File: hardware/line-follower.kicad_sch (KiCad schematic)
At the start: 45 parts, among them J1 AVR-ISP-6, U1 QRE1113GR, U10 QRE1113GR, U11 ATmega2560-16A, U2 QRE1113GR, U3 QRE1113GR, U4 QRE1113GR, U5 QRE1113GR, U6 QRE1113GR, U7 QRE1113GR, U8 QRE1113GR, U9 QRE1113GR

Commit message: add hole for fan
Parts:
- J1: footprint (none) -> Connector_PinHeader_2.54mm:PinHeader_2x03_P2.54mm_Vertical
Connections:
- net +5V: now also J1.2 (VCC)
- net GND: now also J1.6 (GND), U11.11 (GND), U11.32 (GND), U11.62 (GND), U11.81 (GND), U11.99 (GND)
- net at U11.10 (VCC), U11.31 (VCC), U11.61 (VCC)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: now also C11.2, C12.2, C13.2
- net SCK: now reaches U11.20 (PB1)
- net SCK: now also J1.3 (SCK)
- net MOSI: now reaches U11.21 (PB2)
- net MOSI: now also J1.4 (MOSI)
- net MISO: now reaches U11.22 (PB3)
- net MISO: now also J1.1 (MISO)
- net RESET: now reaches U11.30 (~{RESET})
- net RESET: now also J1.5 (~{RST})
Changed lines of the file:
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@@
 (kicad_sch (version 20230121) (generator eeschema)
   (paper "A4")
+  (junction (at 50.8 24.13) (diameter 0) (color 0 0 0 0)
+  )
   (junction (at 226.06 62.23) (diameter 0) (color 0 0 0 0)
   )
+  (junction (at 59.69 24.13) (diameter 0) (color 0 0 0 0)
+  )
   (junction (at 269.24 62.23) (diameter 0) (color 0 0 0 0)
   )
@@
   (junction (at 182.88 62.23) (diameter 0) (color 0 0 0 0)
   )
+  (junction (at 41.91 24.13) (diameter 0) (color 0 0 0 0)
+  )
   (junction (at 269.24 29.21) (diameter 0) (color 0 0 0 0)
   )
@@
     (stroke (width 0) (type default))
   )
+  (wire (pts (xy 67.31 24.13) (xy 67.31 33.02))
+    (stroke (width 0) (type default))
+  )
   (wire (pts (xy 165.1 29.21) (xy 166.37 29.21))
     (stroke (width 0) (type default))
@@
     (stroke (width 0) (type default))
   )
+  (wire (pts (xy 114.3 21.59) (xy 119.38 21.59))
+    (stroke (width 0) (type default))
+  )
   (wire (pts (xy 269.24 87.63) (xy 269.24 88.9))
     (stroke (width 0) (type default))
@@
     (stroke (width 0) (type default))
   )
+  (wire (pts (xy 142.24 21.59) (xy 146.05 21.59))
+    (stroke (width 0) (type default))
+  )
   (wire (pts (xy 224.79 67.31) (xy 227.33 67.31))
     (stroke (width 0) (type default))
@@
     (stroke (width 0) (type default))
   )
+  (wire (pts (xy 59.69 24.13) (xy 67.31 24.13))
+    (stroke (width 0) (type default))
+  )
   (wire (pts (xy 275.59 95.25) (xy 276.86 95.25))
     (stroke (width 0) (type default))
@@
     (stroke (width 0) (type default))
   )
+  (wire (pts (xy 114.3 25.4) (xy 114.3 21.59))
+    (stroke (width 0) (type default))
+  )
   (wire (pts (xy 269.24 54.61) (xy 269.24 55.88))
     (stroke (width 0) (type default))
@@
     (stroke (width 0) (type default))
   )
+  (wire (pts (xy 41.91 24.13) (xy 50.8 24.13))
+    (stroke (width 0) (type default))
+  )
   (wire (pts (xy 252.73 100.33) (xy 250.19 100.33))
     (stroke (width 0) (type default))
@@
     (stroke (width 0) (type default))
   )
+  (wire (pts (xy 41.91 24.13) (xy 39.37 24.13))
+    (stroke (width 0) (type default))
+  )
   (wire (pts (xy 207.01 100.33) (xy 207.01 101.6))
     (stroke (width 0) (type default))
@@
     (stroke (width 0) (type default))
   )
+  (wire (pts (xy 146.05 21.59) (xy 146.05 19.05))
+    (stroke (width 0) (type default))
+  )
   (wire (pts (xy 158.75 54.61) (xy 158.75 62.23))
     (stroke (width 0) (type default))
   )
+  (wire (pts (xy 39.37 20.32) (xy 39.37 24.13))
+    (stroke (width 0) (type default))
+  )
   (wire (pts (xy 250.19 34.29) (xy 250.19 35.56))
     (stroke (width 0) (type default))
@@
   )
   (wire (pts (xy 201.93 62.23) (xy 203.2 62.23))
+    (stroke (width 0) (type default))
+  )
+  (wire (pts (xy 50.8 24.13) (xy 59.69 24.13))
     (stroke (width 0) (type default))
   )
@@
     )
   )
+  (global_label "MISO" (shape input) (at 134.62 34.29 270) (fields_autoplaced)
+    (effects (font (size 1.27 1.27)) (justify right))
+    (property "Intersheetrefs" "${INTERSHEET_REFS}" (at 134.62 41.792 90)
+      (effects (font (size 1.27 1.27)) (justify right) hide)
+    )
+  )
   (global_label "OUT7" (shape input) (at 233.68 95.25 0) (fields_autoplaced)
     (effects (font (size 1.27 1.27)) (justify left))
@@
     )
   )
+  (global_label "MOSI" (shape input) (at 87.63 68.58 0) (fields_autoplaced)
+    (effects (font (size 1.27 1.27)) (justify left))
+    (property "Intersheetrefs" "${INTERSHEET_REFS}" (at 95.132 68.58 0)
+      (effects (font (size 1.27 1.27)) (justify left) hide)
+    )
+  )
   (global_label "OUT6" (shape input) (at 233.68 62.23 0) (fields_autoplaced)
     (effects (font (size 1.27 1.27)) (justify left))
@@
     )
   )
+  (global_label "MISO" (shape input) (at 87.63 71.12 0) (fields_autoplaced)
+    (effects (font (size 1.27 1.27)) (justify left))
+    (property "Intersheetrefs" "${INTERSHEET_REFS}" (at 95.132 71.12 0)
+      (effects (font (size 1.27 1.27)) (justify left) hide)
+    )
+  )
   (global_label "OUT3" (shape input) (at 276.86 95.25 0) (fields_autoplaced)
     (effects (font (size 1.27 1.27)) (justify left))
@@
     )
   )
+  (global_label "MOSI" (shape input) (at 132.08 34.29 270) (fields_autoplaced)
+    (effects (font (size 1.27 1.27)) (justify right))
+    (property "Intersheetrefs" "${INTERSHEET_REFS}" (at 132.08 41.792 90)
+      (effects (font (size 1.27 1.27)) (justify right) hide)
+    )
+  )
   (global_label "OUT8" (shape input) (at 233.68 128.27 0) (fields_autoplaced)
     (effects (font (size 1.27 1.27)) (justify left))
@@
     )
   )
+  (global_label "RESET" (shape input) (at 46.99 40.64 180) (fields_autoplaced)
+    (effects (font (size 1.27 1.27)) (justify right))
+    (property "Intersheetrefs" "${INTERSHEET_REFS}" (at 38.3391 40.64 0)
+      (effects (font (size 1.27 1.27)) (justify right) hide)
+    )
+  )
   (global_label "OUT5" (shape input) (at 87.63 165.1 0) (fields_autoplaced)
     (effects (font (size 1.27 1.27)) (justify left))
@@
     )
   )
+  (global_label "SCK" (shape input) (at 129.54 34.29 270) (fields_autoplaced)
+    (effects (font (size 1.27 1.27)) (justify right))
+    (property "Intersheetrefs" "${INTERSHEET_REFS}" (at 129.54 40.9453 90)
+      (effects (font (size 1.27 1.27)) (justify right) hide)
+    )
+  )
+  (global_label "SCK" (shape input) (at 87.63 66.04 0) (fields_autoplaced)
+    (effects (font (size 1.27 1.27)) (justify left))
+    (property "Intersheetrefs" "${INTERSHEET_REFS}" (at 94.2853 66.04 0)
+      (effects (font (size 1.27 1.27)) (justify left) hide)
+    )
+  )
   (global_label "OUT9" (shape input) (at 190.5 29.21 0) (fields_autoplaced)
     (effects (font (size 1.27 1.27)) (justify left))
     (property "Intersheetrefs" "${INTERSHEET_REFS}" (at 198.2439 29.21 0)
       (effects (font (size 1.27 1.27)) (justify left) hide)
+    )
+  )
+  (global_label "RESET" (shape input) (at 127 34.29 270) (fields_autoplaced)
+    (effects (font (size 1.27 1.27)) (justify right))
+    (property "Intersheetrefs" "${INTERSHEET_REFS}" (at 127 42.9409 90)
+      (effects (font (size 1.27 1.27)) (justify right) hide)
     )
   )
@@
       (effects (font (size 1.27 1.27)))
     )
-    (property "Footprint" "" (at 130.81 17.78 90)
+    (property "Footprint" "Connector_PinHeader_2.54mm:PinHeader_2x03_P2.54mm_Vertical" (at 130.81 17.78 90)
       (effects (font (size 1.27 1.27)) hide)
     )
@@
     )
   )
+  (symbol (lib_id "power:GND") (at 114.3 25.4 0) (unit 1)
+    (in_bom yes) (on_board yes) (dnp no) (fields_autoplaced)
+    (property "Reference" "#PWR042" (at 114.3 31.75 0)
+      (effects (font (size 1.27 1.27)) hide)
+    )
+    (property "Value" "GND" (at 114.3 30.48 0)
+      (effects (font (size 1.27 1.27)))
+    )
+    (property "Footprint" "" (at 114.3 25.4 0)
+      (effects (font (size 1.27 1.27)) hide)
+    )
+    (property "Datasheet" "" (at 114.3 25.4 0)
+      (effects (font (size 1.27 1.27)) hide)
+    )
+    (pin "1")
+    (instances
+      (project "line-follower"
+        (path "/16c7c831-eafb-4a0a-afab-2bf2c115b426"
+          (reference "#PWR042") (unit 1)
+        )
+      )
+    )
+  )
   (symbol (lib_id "power:GND") (at 163.83 35.56 0) (unit 1)
     (in_bom yes) (on_board yes) (dnp no) (fields_autoplaced)
@@
     )
   )
+  (symbol (lib_id "power:+5V") (at 146.05 19.05 0) (unit 1)
+    (in_bom yes) (on_board yes) (dnp no) (fields_autoplaced)
+    (property "Reference" "#PWR041" (at 146.05 22.86 0)
+      (effects (font (size 1.27 1.27)) hide)
+    )
+    (property "Value" "+5V" (at 146.05 13.97 0)
+      (effects (font (size 1.27 1.27)))
+    )
+    (property "Footprint" "" (at 146.05 19.05 0)
+      (effects (font (size 1.27 1.27)) hide)
+    )
+    (property "Datasheet" "" (at 146.05 19.05 0)
+      (effects (font (size 1.27 1.27)) hide)
+    )
+    (pin "1")
+    (instances
+      (project "line-follower"
+        (path "/16c7c831-eafb-4a0a-afab-2bf2c115b426"
+          (reference "#PWR041") (unit 1)
+        )
+      )
+    )
+  )
   (symbol (lib_id "power:+5V") (at 226.06 120.65 0) (unit 1)
     (in_bom yes) (on_board yes) (dnp no) (fields_autoplaced)
@@
         )
       )
+    )
+  )
+  (symbol (lib_id "power:GND") (at 67.31 180.34 0) (unit 1)
+    (in_bom yes) (on_board yes) (dnp no) (fields_autoplaced)
+    (property "Reference" "#PWR043" (at 67.31 186.69 0)
+      (effects (font (size 1.27 1.27)) hide)
+    )
+    (property "Value" "GND" (at 67.31 185.42 0)
+      (effects (font (size 1.27 1.27)))
+    )
+    (property "Footprint" "" (at 67.31 180.34 0)
+      (effects (font (size 1.27 1.27)) hide)
+    )
+    (property "Datasheet" "" (at 67.31 180.34 0)
+      (effects (font (size 1.27 1.27)) hide)
+    )
+    (pin "1")
+    (instances
+      (project "line-follower"
+        (path "/16c7c831-eafb-4a0a-afab-2bf2c115b426"
+          (reference "#PWR043") (unit 1)
+        )
+      )

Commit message: add regulator
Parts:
- added C14, C15, C21: C_Polarized_Small, Capacitor_SMD:CP_Elec_6.3x4.9, symbol Device:C_Polarized_Small
- added C16, C17: 20p, Capacitor_SMD:C_0603_1608Metric, symbol Device:C_Small
- added C18, C19, C20: 10nF, Capacitor_SMD:C_0603_1608Metric, symbol Device:C_Small
- added D1: 1N5819, Diode_THT:D_DO-41_SOD81_P10.16mm_Horizontal, symbol Diode:1N5819
- added J2, J3: Conn_01x02, Connector_PinSocket_2.54mm:PinSocket_1x02_P2.54mm_Vertical, symbol Connector_Generic:Conn_01x02
- added J4: Conn_01x02, Connector_PinHeader_2.54mm:PinHeader_1x02_P2.54mm_Vertical, symbol Connector_Generic:Conn_01x02
- added Q1: Si2319CDS, Package_TO_SOT_SMD:SOT-23, symbol Transistor_FET:Si2319CDS
- added R21: 1M, Resistor_SMD:R_0603_1608Metric, symbol Device:R_Small
- added R22, R23: R_Small, Resistor_SMD:R_0603_1608Metric, symbol Device:R_Small
- added U12: MX1508, Package_SO:SOIC-16W_5.3x10.2mm_P1.27mm, symbol MX1508:MX1508
- added U13: LM317_SOT-223, Package_TO_SOT_SMD:SOT-223-3_TabPin2, symbol Regulator_Linear:LM317_SOT-223
- added Y1: Crystal, Crystal:Crystal_SMD_HC49-SD, symbol Device:Crystal
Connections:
- net +5V: now also C11.2, C12.2, C13.2, U11.10 (VCC), U11.100 (AVCC), U11.31 (VCC), U11.61 (VCC), U11.80 (VCC), C14.1, C15.1, C18.2, C19.2, U12.1 (VCC1), U12.4 (VDD1), U12.5 (VCC2), U12.8 (VDD2), U13.2 (VO)
- net GND: now also C11.1, C12.1, C13.1, C14.2, C15.2, C16.2, C17.2, C18.1, C19.1, C20.1, C21.2, Q1.2 (S), R23.2, U12.10 (AGND2), U12.11 (PGND2), U12.14 (AGND1), U12.15 (PGND1), U13.1 (ADJ)
- net MOTOR_L_A: now reaches U11.15 (PH3)
- net MOTOR_L_A: now also U12.2 (INA1)
- net MOTOR_L_B: now reaches U11.16 (PH4)
- net MOTOR_L_B: now also U12.3 (INB1)
- net MOTOR_R_A: now reaches U11.17 (PH5)
- net MOTOR_R_A: now also U12.6 (INA2)
- net MOTOR_R_B: now reaches U11.18 (PH6)
- net MOTOR_R_B: now also U12.7 (INB2)
- net MOTOR_1: now reaches U11.23 (PB4)
- net MOTOR_1: now also R22.1
- net OSOUT: now reaches U11.33 (XTAL2)
- net OSOUT: now also C17.1, R21.2, Y1.1
- net OSIN: now reaches U11.34 (XTAL1)
- net OSIN: now also C16.1, R21.1, Y1.2
- new net: J2.2 (Pin_2), U12.13 (OUTB1)
- new net: J2.1 (Pin_1), U12.16 (OUTA1)
- new net: D1.2 (A), J4.2 (Pin_2), Q1.3 (D)
- new net: J3.1 (Pin_1), U12.12 (OUTA2)
- new net: J3.2 (Pin_2), U12.9 (OUTB2)
- new net: Q1.1 (G), R22.2, R23.1
- new net +BATT: C20.2, C21.1, D1.1 (K), J4.1 (Pin_1), U13.3 (VI)
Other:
- note added: "5V regulator"
- note added: "FAN CONTROL"
- note added: "MCU"
- note added: "MCU OSCILATOR"
- note added: "MOTOR CONTROL"
- note added: "PROGRAMING PORT"
- moved on the sheet: C1, C10, C11, C12, C13, C2, C3, C4, C5, C6, C7, C8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

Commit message: add battery connector
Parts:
- added D2, D3, D4, D5, D6, D7: LED, LED_SMD:LED_0603_1608Metric, symbol Device:LED
- added J5: Conn_01x02, Connector_TE-Connectivity:TE_826576-2_1x02_P3.96mm_Vertical, symbol Connector_Generic:Conn_01x02
- added Q2: 2N7002, Package_TO_SOT_SMD:SOT-23, symbol Transistor_FET:2N7002
- added R24, R25, R26, R27, R28, R29, R31: 2K, Resistor_SMD:R_0603_1608Metric, symbol Device:R_Small
- added R30: 10K, Resistor_SMD:R_0603_1608Metric, symbol Device:R_Small
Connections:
- net +5V: now also Q2.3 (D)
- net +BATT: now also J5.2 (Pin_2)
- net GND: now also J5.1 (Pin_1), R24.2, R25.2, R26.2, R27.2, R28.2, R29.2, R30.2
- net F_LED: now reaches U11.87 (PK2)
- net F_LED: now also R31.2
- new net: D4.1 (K), R26.1
- new net: D2.2 (A), D3.2 (A), D4.2 (A), D5.2 (A), D6.2 (A), D7.2 (A), Q2.2 (S)
- new net: D6.1 (K), R28.1
- new net: D5.1 (K), R27.1
- new net: D3.1 (K), R25.1
- new net: D7.1 (K), R29.1
- new net: Q2.1 (G), R30.1, R31.1
- new net: D2.1 (K), R24.1
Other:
- moved on the sheet: C14, C15, C16, C17, J2, J3, R21, U12A, U12B, Y1

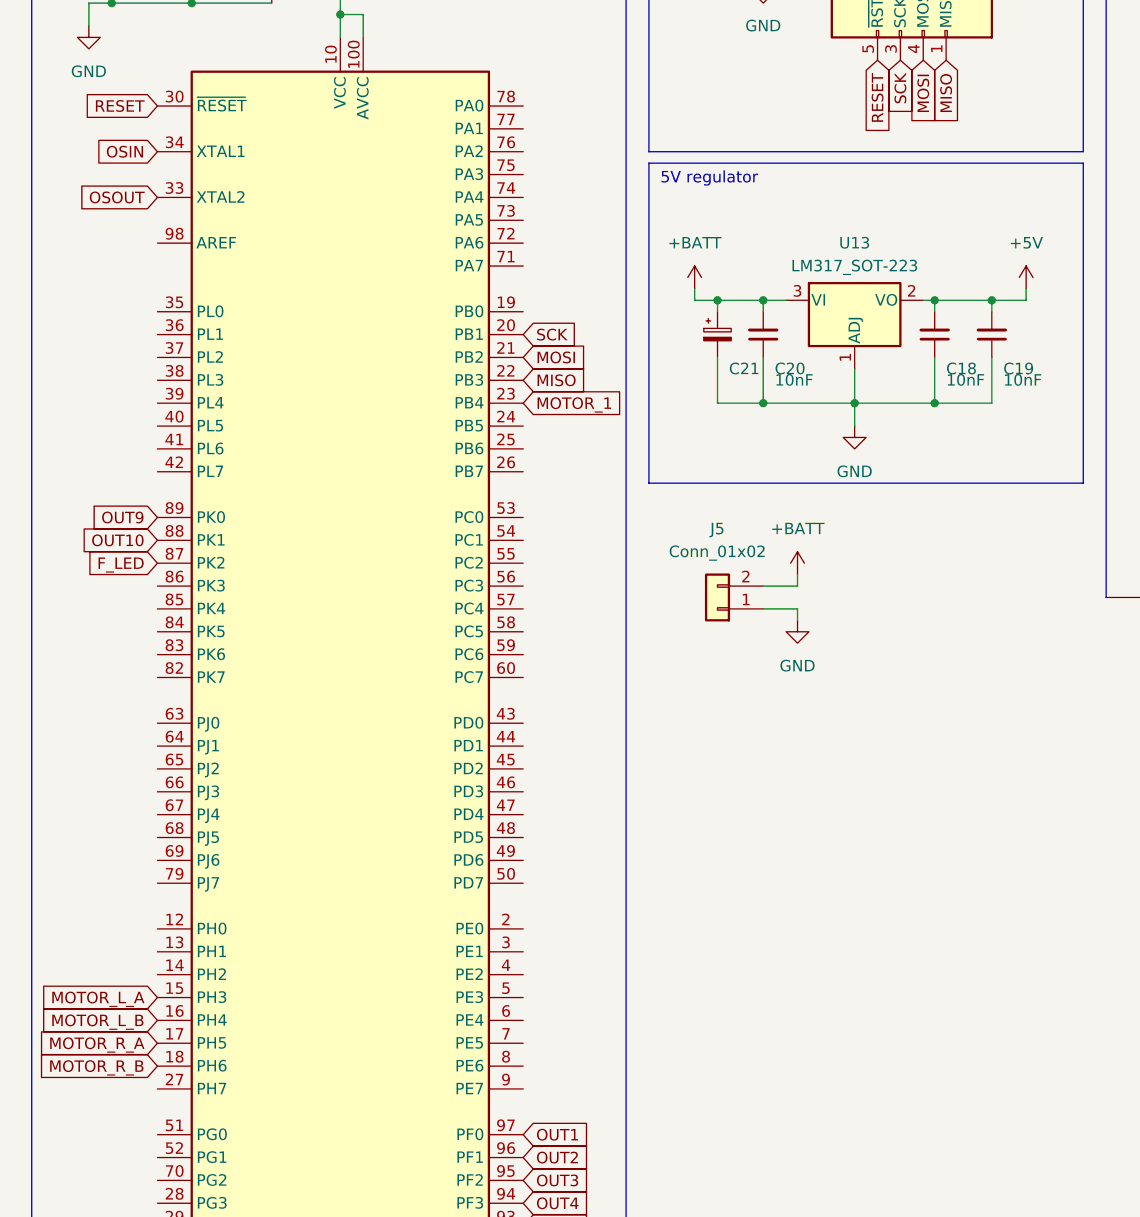
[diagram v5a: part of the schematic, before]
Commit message: add led + switch
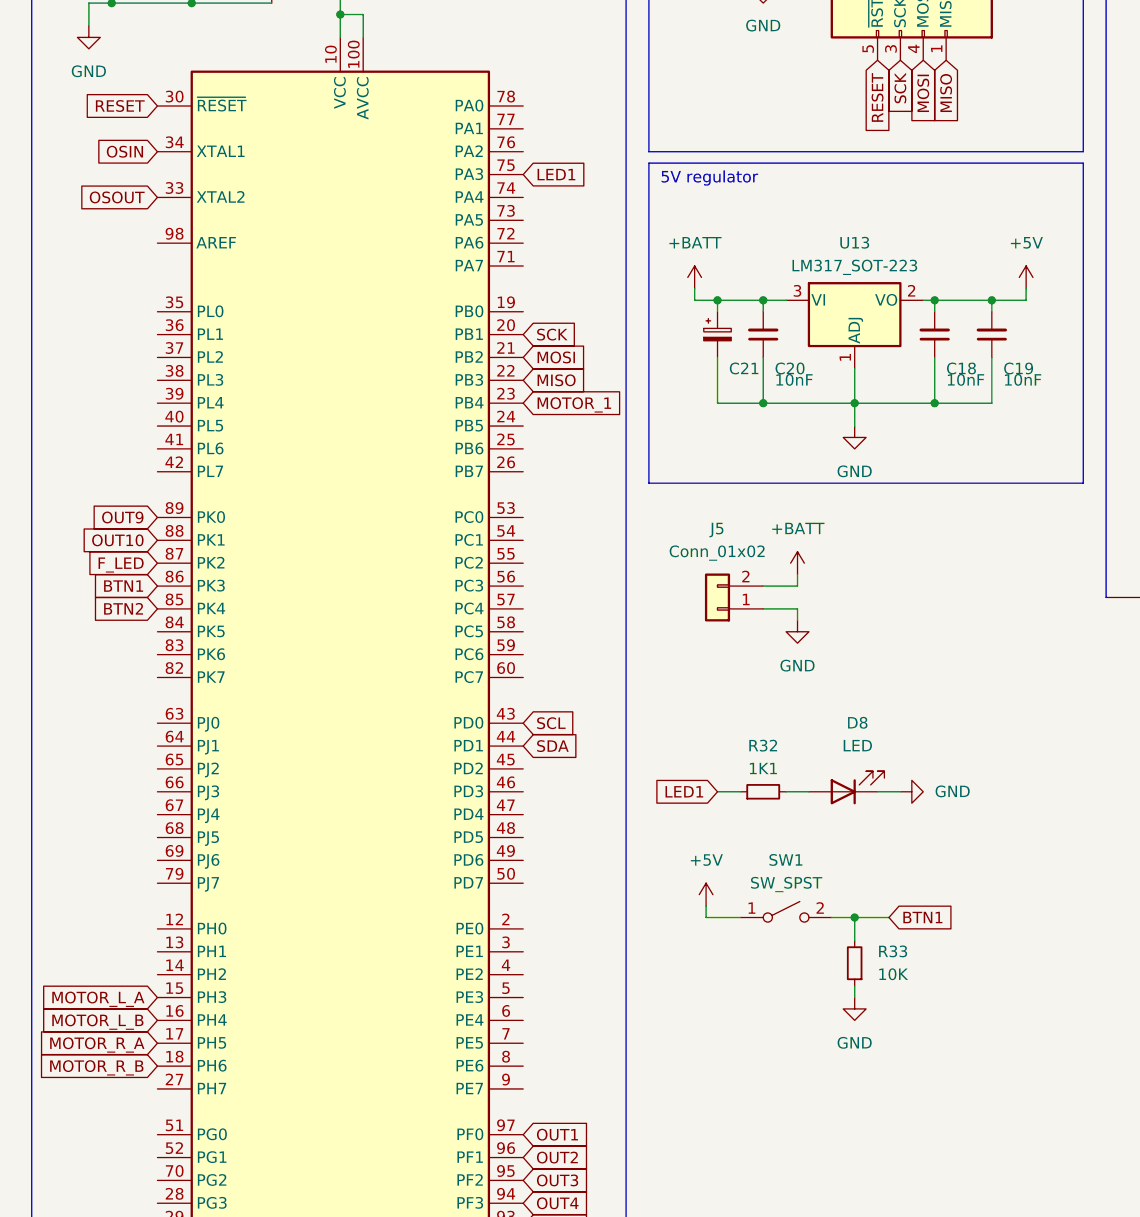
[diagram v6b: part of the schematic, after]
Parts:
- added D8: LED, LED_SMD:LED_0603_1608Metric, symbol Device:LED
- added R32: 1K1, Resistor_SMD:R_0603_1608Metric, symbol Device:R_Small
- added R33: 10K, Resistor_SMD:R_0603_1608Metric, symbol Device:R_Small
- added SW1: SW_SPST, Button_Switch_SMD:SW_SPST_FSMSM, symbol Switch:SW_SPST
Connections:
- net +5V: now also SW1.1 (A)
- net GND: now also D8.1 (K), R33.1
- net SCL: now reaches U11.43 (PD0)
- net SDA: now reaches U11.44 (PD1)
- net LED1: now reaches U11.75 (PA3)
- net LED1: now also R32.1
- net BTN2: now reaches U11.85 (PK4)
- net BTN1: now reaches U11.86 (PK3)
- net BTN1: now also R33.2, SW1.2 (B)
- new net: D8.2 (A), R32.2
